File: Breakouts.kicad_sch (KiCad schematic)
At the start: 11 parts, among them J1 Conn_01x08, J2 Conn_01x08, J3 Conn_01x08, J4 Conn_01x08, J5 Conn_02x04_Odd_Even, J6 Conn_01x06, J7 Conn_01x06, K1 G5LE-1, U1 ESP-07, U2 AMS1117-3_3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

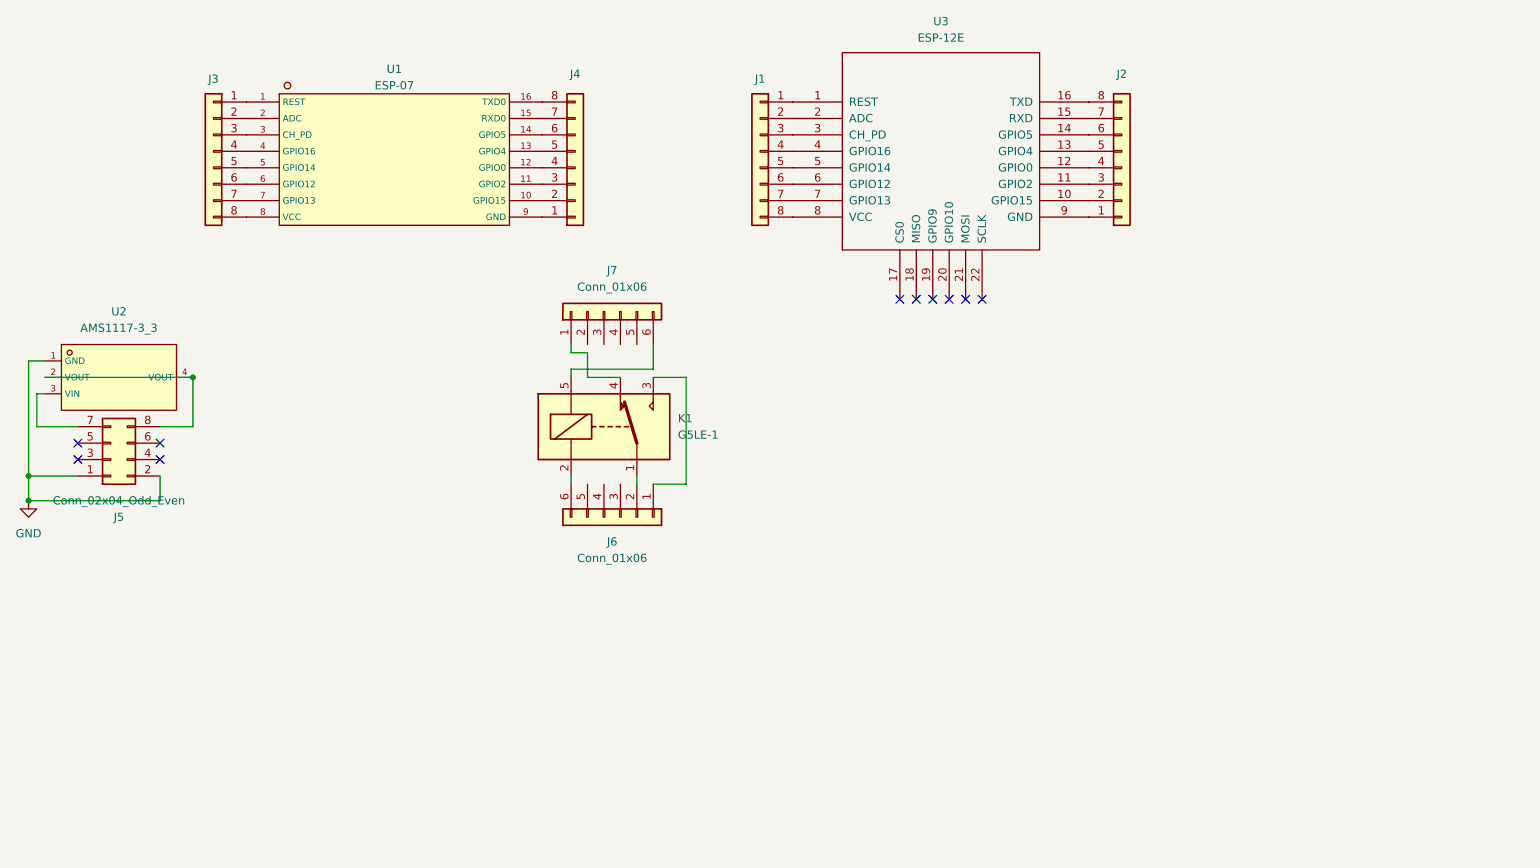
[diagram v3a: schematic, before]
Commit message: Add audio jack
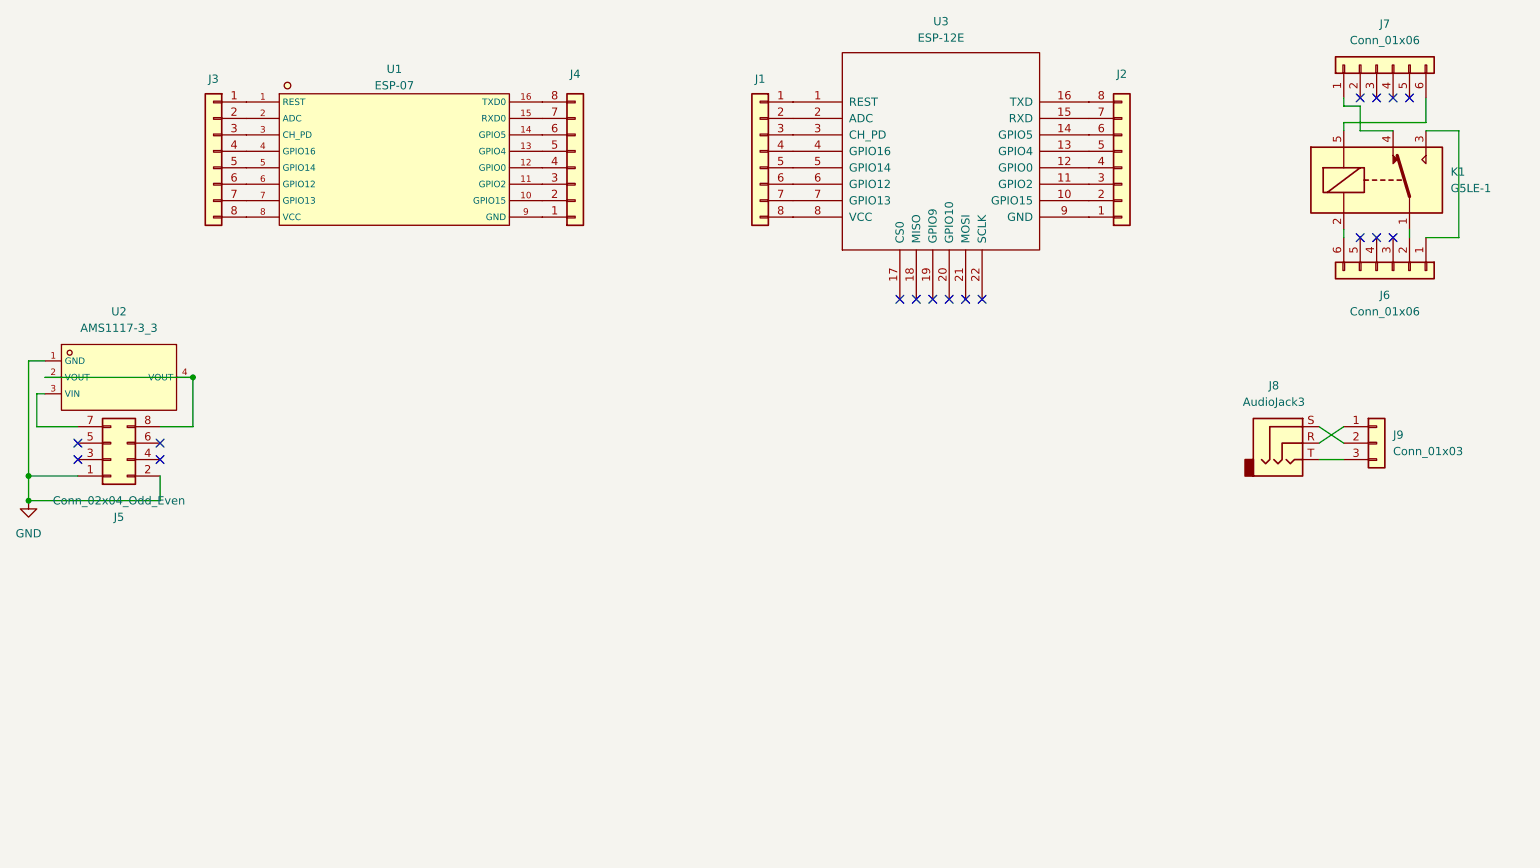
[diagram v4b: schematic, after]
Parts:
- added J8: AudioJack3, Connector_Audio:Jack_3.5mm_CUI_SJ-3523-SMT_Horizontal, symbol Connector_Audio:AudioJack3
- added J9: Conn_01x03, Connector_PinHeader_2.54mm:PinHeader_1x03_P2.54mm_Vertical, symbol Connector_Generic:Conn_01x03
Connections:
- new net: J8.R, J9.1 (Pin_1)
- new net: J8.S, J9.2 (Pin_2)
- new net: J8.T, J9.3 (Pin_3)
- no-connect marks 10 -> 17
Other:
- moved on the sheet: J6, J7, K1
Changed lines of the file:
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@@
   )
   (no_connect (at 193.04 59.055))
+  (no_connect (at 261.62 49.53))
+  (no_connect (at 261.62 27.94))
   (no_connect (at 63.5 83.82))
   (no_connect (at 76.2 81.28))
+  (no_connect (at 264.16 27.94))
   (no_connect (at 63.5 81.28))
   (no_connect (at 203.2 59.055))
+  (no_connect (at 269.24 27.94))
   (no_connect (at 76.2 83.82))
   (no_connect (at 190.5 59.055))
+  (no_connect (at 264.16 49.53))
   (no_connect (at 200.66 59.055))
   (no_connect (at 195.58 59.055))
+  (no_connect (at 266.7 49.53))
+  (no_connect (at 266.7 27.94))
   (no_connect (at 198.12 59.055))
-  (wire (pts (xy 139.7 67.31) (xy 139.7 66.04))
-    (stroke (width 0) (type default))
-  )
-  (wire (pts (xy 139.7 69.85) (xy 139.7 71.12))
-    (stroke (width 0) (type default))
-  )
-  (wire (pts (xy 142.24 67.31) (xy 139.7 67.31))
+  (wire (pts (xy 259.08 29.21) (xy 259.08 27.94))
+    (stroke (width 0) (type default))
+  )
+  (wire (pts (xy 259.08 31.75) (xy 259.08 33.02))
+    (stroke (width 0) (type default))
+  )
+  (wire (pts (xy 255.27 83.82) (xy 259.08 83.82))
+    (stroke (width 0) (type default))
+  )
+  (wire (pts (xy 261.62 29.21) (xy 259.08 29.21))
     (stroke (width 0) (type default))
   )
@@
     (stroke (width 0) (type default))
   )
-  (wire (pts (xy 152.4 69.85) (xy 139.7 69.85))
-    (stroke (width 0) (type default))
-  )
-  (wire (pts (xy 147.32 71.12) (xy 142.24 71.12))
+  (wire (pts (xy 271.78 31.75) (xy 259.08 31.75))
+    (stroke (width 0) (type default))
+  )
+  (wire (pts (xy 266.7 33.02) (xy 261.62 33.02))
     (stroke (width 0) (type default))
   )
@@
     (stroke (width 0) (type default))
   )
+  (wire (pts (xy 259.08 78.74) (xy 255.27 81.28))
+    (stroke (width 0) (type default))
+  )
   (wire (pts (xy 55.88 90.17) (xy 76.2 90.17))
     (stroke (width 0) (type default))
   )
-  (wire (pts (xy 142.24 71.12) (xy 142.24 67.31))
-    (stroke (width 0) (type default))
-  )
-  (wire (pts (xy 152.4 71.12) (xy 157.48 71.12))
+  (wire (pts (xy 261.62 33.02) (xy 261.62 29.21))
+    (stroke (width 0) (type default))
+  )
+  (wire (pts (xy 271.78 33.02) (xy 276.86 33.02))
     (stroke (width 0) (type default))
   )
@@
     (stroke (width 0) (type default))
   )
-  (wire (pts (xy 139.7 86.36) (xy 139.7 87.63))
+  (wire (pts (xy 259.08 48.26) (xy 259.08 49.53))
     (stroke (width 0) (type default))
   )
@@
     (stroke (width 0) (type default))
   )
-  (wire (pts (xy 157.48 71.12) (xy 157.48 87.63))
-    (stroke (width 0) (type default))
-  )
-  (wire (pts (xy 149.86 86.36) (xy 149.86 87.63))
-    (stroke (width 0) (type default))
-  )
-  (wire (pts (xy 152.4 66.04) (xy 152.4 69.85))
+  (wire (pts (xy 276.86 33.02) (xy 276.86 49.53))
+    (stroke (width 0) (type default))
+  )
+  (wire (pts (xy 269.24 48.26) (xy 269.24 49.53))
+    (stroke (width 0) (type default))
+  )
+  (wire (pts (xy 271.78 27.94) (xy 271.78 31.75))
     (stroke (width 0) (type default))
   )
@@
     (stroke (width 0) (type default))
   )
-  (wire (pts (xy 157.48 87.63) (xy 152.4 87.63))
+  (wire (pts (xy 276.86 49.53) (xy 271.78 49.53))
+    (stroke (width 0) (type default))
+  )
+  (wire (pts (xy 255.27 78.74) (xy 259.08 81.28))
     (stroke (width 0) (type default))
   )
@@
         (path "/7ebf650a-1c0b-4d71-8ef1-c883cde2ac89"
           (reference "U2") (unit 1)
+        )
+      )
+    )
+  )
+  (symbol (lib_id "Connector_Generic:Conn_01x03") (at 264.16 81.28 0) (unit 1)
+    (in_bom yes) (on_board yes) (dnp no) (fields_autoplaced)
+    (property "Reference" "J9" (at 266.7 80.01 0)
+      (effects (font (size 1.27 1.27)) (justify left))
+    )
+    (property "Value" "Conn_01x03" (at 266.7 82.55 0)
+      (effects (font (size 1.27 1.27)) (justify left))
+    )
+    (property "Footprint" "Connector_PinHeader_2.54mm:PinHeader_1x03_P2.54mm_Vertical" (at 264.16 81.28 0)
+      (effects (font (size 1.27 1.27)) hide)
+    )
+    (property "Datasheet" "~" (at 264.16 81.28 0)
+      (effects (font (size 1.27 1.27)) hide)
+    )
+    (pin "1")
+    (pin "3")
+    (pin "2")
+    (instances
+      (project "Breakouts"
+        (path "/7ebf650a-1c0b-4d71-8ef1-c883cde2ac89"
+          (reference "J9") (unit 1)
         )
       )
@@
     )
   )
-  (symbol (lib_id "Connector_Generic:Conn_01x06") (at 147.32 92.71 270) (unit 1)
-    (in_bom yes) (on_board yes) (dnp no) (fields_autoplaced)
-    (property "Reference" "J6" (at 146.05 96.52 90)
-      (effects (font (size 1.27 1.27)))
-    )
-    (property "Value" "Conn_01x06" (at 146.05 99.06 90)
-      (effects (font (size 1.27 1.27)))
-    )
-    (property "Footprint" "Connector_PinHeader_2.54mm:PinHeader_1x06_P2.54mm_Vertical" (at 147.32 92.71 0)
-      (effects (font (size 1.27 1.27)) hide)
-    )
-    (property "Datasheet" "~" (at 147.32 92.71 0)
+  (symbol (lib_id "Connector_Generic:Conn_01x06") (at 266.7 54.61 270) (unit 1)
+    (in_bom yes) (on_board yes) (dnp no) (fields_autoplaced)
+    (property "Reference" "J6" (at 265.43 58.42 90)
+      (effects (font (size 1.27 1.27)))
+    )
+    (property "Value" "Conn_01x06" (at 265.43 60.96 90)
+      (effects (font (size 1.27 1.27)))
+    )
+    (property "Footprint" "Connector_PinHeader_2.54mm:PinHeader_1x06_P2.54mm_Vertical" (at 266.7 54.61 0)
+      (effects (font (size 1.27 1.27)) hide)
+    )
+    (property "Datasheet" "~" (at 266.7 54.61 0)
       (effects (font (size 1.27 1.27)) hide)
     )
@@
     )
   )
-  (symbol (lib_id "Relay:G5LE-1") (at 144.78 78.74 0) (unit 1)
+  (symbol (lib_id "Relay:G5LE-1") (at 264.16 40.64 0) (unit 1)
     (in_bom no) (on_board yes) (dnp no) (fields_autoplaced)
-    (property "Reference" "K1" (at 156.21 77.47 0)
+    (property "Reference" "K1" (at 275.59 39.37 0)
       (effects (font (size 1.27 1.27)) (justify left))
     )
-    (property "Value" "G5LE-1" (at 156.21 80.01 0)
+    (property "Value" "G5LE-1" (at 275.59 41.91 0)
       (effects (font (size 1.27 1.27)) (justify left))
     )
-    (property "Footprint" "Relay_THT:Relay_SPDT_Omron-G5LE-1" (at 156.21 80.01 0)
+    (property "Footprint" "Relay_THT:Relay_SPDT_Omron-G5LE-1" (at 275.59 41.91 0)
       (effects (font (size 1.27 1.27)) (justify left) hide)
     )
-    (property "Datasheet" "http://www.omron.com/ecb/products/pdf/en-g5le.pdf" (at 144.78 78.74 0)
+    (property "Datasheet" "http://www.omron.com/ecb/products/pdf/en-g5le.pdf" (at 264.16 40.64 0)
       (effects (font (size 1.27 1.27)) hide)
     )
@@
     )
   )
-  (symbol (lib_id "Connector_Generic:Conn_01x06") (at 144.78 60.96 90) (unit 1)
-    (in_bom yes) (on_board yes) (dnp no) (fields_autoplaced)
-    (property "Reference" "J7" (at 146.05 54.61 90)
-      (effects (font (size 1.27 1.27)))
-    )
-    (property "Value" "Conn_01x06" (at 146.05 57.15 90)
-      (effects (font (size 1.27 1.27)))
-    )
-    (property "Footprint" "Connector_PinHeader_2.54mm:PinHeader_1x06_P2.54mm_Vertical" (at 144.78 60.96 0)
-      (effects (font (size 1.27 1.27)) hide)
-    )
-    (property "Datasheet" "~" (at 144.78 60.96 0)
+  (symbol (lib_id "Connector_Generic:Conn_01x06") (at 264.16 22.86 90) (unit 1)
+    (in_bom yes) (on_board yes) (dnp no) (fields_autoplaced)
+    (property "Reference" "J7" (at 265.43 16.51 90)
+      (effects (font (size 1.27 1.27)))
+    )
+    (property "Value" "Conn_01x06" (at 265.43 19.05 90)
+      (effects (font (size 1.27 1.27)))
+    )
+    (property "Footprint" "Connector_PinHeader_2.54mm:PinHeader_1x06_P2.54mm_Vertical" (at 264.16 22.86 0)
+      (effects (font (size 1.27 1.27)) hide)
+    )
+    (property "Datasheet" "~" (at 264.16 22.86 0)
       (effects (font (size 1.27 1.27)) hide)
     )
@@
         )
       )
+    )
+  )
+  (symbol (lib_id "Connector_Audio:AudioJack3") (at 250.19 81.28 0) (unit 1)
+    (in_bom yes) (on_board yes) (dnp no) (fields_autoplaced)
+    (property "Reference" "J8" (at 248.285 72.39 0)
+      (effects (font (size 1.27 1.27)))
+    )
+    (property "Value" "AudioJack3" (at 248.285 74.93 0)
+      (effects (font (size 1.27 1.27)))
+    )
+    (property "Footprint" "Connector_Audio:Jack_3.5mm_CUI_SJ-3523-SMT_Horizontal" (at 250.19 81.28 0)
+      (effects (font (size 1.27 1.27)) hide)
+    )
+    (property "Datasheet" "~" (at 250.19 81.28 0)
+      (effects (font (size 1.27 1.27)) hide)
+    )
+    (pin "T")
+    (pin "R")
+    (pin "S")
+    (instances
+      (project "Breakouts"
+        (path "/7ebf650a-1c0b-4d71-8ef1-c883cde2ac89"
+          (reference "J8") (unit 1)
+        )
+      )

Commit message: big audio jack
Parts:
- added J10: AudioJack3_Switch, Connector_Audio:Jack_6.35mm_Neutrik_NMJ6HFD2_Horizontal, symbol Connector_Audio:AudioJack3_Switch
- added J11, J12: Conn_01x03, Connector_PinHeader_2.54mm:PinHeader_1x03_P2.54mm_Vertical_SMD_Pin1Left, symbol Connector_Generic:Conn_01x03
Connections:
- new net: J10.S, J11.1 (Pin_1)
- new net: J10.R, J11.2 (Pin_2)
- new net: J10.T, J11.3 (Pin_3)
- new net: J10.TN, J12.1 (Pin_1)
- new net: J10.RN, J12.2 (Pin_2)
- new net: J10.SN, J12.3 (Pin_3)
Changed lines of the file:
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@@
+    (stroke (width 0) (type default))
+  )
+  (wire (pts (xy 214.63 102.87) (xy 217.17 102.87))
     (stroke (width 0) (type default))
   )
@@
     (stroke (width 0) (type default))
   )
+  (wire (pts (xy 218.44 97.79) (xy 218.44 105.41))
+    (stroke (width 0) (type default))
+  )
+  (wire (pts (xy 222.25 92.71) (xy 222.25 95.25))
+    (stroke (width 0) (type default))
+  )
   (wire (pts (xy 57.15 78.74) (xy 57.15 73.66))
     (stroke (width 0) (type default))
@@
     (stroke (width 0) (type default))
   )
+  (wire (pts (xy 218.44 105.41) (xy 224.79 105.41))
+    (stroke (width 0) (type default))
+  )
+  (wire (pts (xy 224.79 100.33) (xy 214.63 100.33))
+    (stroke (width 0) (type default))
+  )
+  (wire (pts (xy 222.25 95.25) (xy 214.63 95.25))
+    (stroke (width 0) (type default))
+  )
+  (wire (pts (xy 214.63 97.79) (xy 218.44 97.79))
+    (stroke (width 0) (type default))
+  )
+  (wire (pts (xy 217.17 107.95) (xy 224.79 107.95))
+    (stroke (width 0) (type default))
+  )
   (wire (pts (xy 58.42 68.58) (xy 55.88 68.58))
     (stroke (width 0) (type default))
   )
+  (wire (pts (xy 219.71 102.87) (xy 224.79 102.87))
+    (stroke (width 0) (type default))
+  )
   (wire (pts (xy 57.15 73.66) (xy 58.42 73.66))
     (stroke (width 0) (type default))
@@
     (stroke (width 0) (type default))
   )
+  (wire (pts (xy 224.79 92.71) (xy 222.25 92.71))
+    (stroke (width 0) (type default))
+  )
   (wire (pts (xy 81.28 78.74) (xy 76.2 78.74))
     (stroke (width 0) (type default))
   )
+  (wire (pts (xy 224.79 95.25) (xy 224.79 100.33))
+    (stroke (width 0) (type default))
+  )
   (wire (pts (xy 58.42 71.12) (xy 81.28 71.12))
     (stroke (width 0) (type default))
   )
+  (wire (pts (xy 224.79 90.17) (xy 214.63 90.17))
+    (stroke (width 0) (type default))
+  )
   (wire (pts (xy 276.86 33.02) (xy 276.86 49.53))
     (stroke (width 0) (type default))
@@
     (stroke (width 0) (type default))
   )
+  (wire (pts (xy 219.71 92.71) (xy 219.71 102.87))
+    (stroke (width 0) (type default))
+  )
   (wire (pts (xy 76.2 90.17) (xy 76.2 86.36))
+    (stroke (width 0) (type default))
+  )
+  (wire (pts (xy 217.17 102.87) (xy 217.17 107.95))
+    (stroke (width 0) (type default))
+  )
+  (wire (pts (xy 214.63 92.71) (xy 219.71 92.71))
     (stroke (width 0) (type default))
   )
@@
     )
   )
+  (symbol (lib_id "Connector_Generic:Conn_01x03") (at 229.87 92.71 0) (unit 1)
+    (in_bom yes) (on_board yes) (dnp no)
+    (property "Reference" "J11" (at 232.41 91.44 0)
+      (effects (font (size 1.27 1.27)) (justify left))
+    )
+    (property "Value" "Conn_01x03" (at 232.41 93.98 0)
+      (effects (font (size 1.27 1.27)) (justify left))
+    )
+    (property "Footprint" "Connector_PinHeader_2.54mm:PinHeader_1x03_P2.54mm_Vertical_SMD_Pin1Left" (at 229.87 92.71 0)
+      (effects (font (size 1.27 1.27)) hide)
+    )
+    (property "Datasheet" "~" (at 229.87 92.71 0)
+      (effects (font (size 1.27 1.27)) hide)
+    )
+    (pin "1")
+    (pin "2")
+    (pin "3")
+    (instances
+      (project "Breakouts"
+        (path "/7ebf650a-1c0b-4d71-8ef1-c883cde2ac89"
+          (reference "J11") (unit 1)
+        )
+      )
+    )
+  )
   (symbol (lib_id "jlc_symbols:ESP-07") (at 112.395 36.195 0) (unit 1)
     (in_bom yes) (on_board yes) (dnp no) (fields_autoplaced)
@@
     )
   )
+  (symbol (lib_id "Connector_Generic:Conn_01x03") (at 229.87 105.41 0) (mirror x) (unit 1)
+    (in_bom yes) (on_board yes) (dnp no)
+    (property "Reference" "J12" (at 232.41 106.68 0)
+      (effects (font (size 1.27 1.27)) (justify left))
+    )
+    (property "Value" "Conn_01x03" (at 232.41 104.14 0)
+      (effects (font (size 1.27 1.27)) (justify left))
+    )
+    (property "Footprint" "Connector_PinHeader_2.54mm:PinHeader_1x03_P2.54mm_Vertical_SMD_Pin1Left" (at 229.87 105.41 0)
+      (effects (font (size 1.27 1.27)) hide)
+    )
+    (property "Datasheet" "~" (at 229.87 105.41 0)
+      (effects (font (size 1.27 1.27)) hide)
+    )
+    (pin "1")
+    (pin "2")
+    (pin "3")
+    (instances
+      (project "Breakouts"
+        (path "/7ebf650a-1c0b-4d71-8ef1-c883cde2ac89"
+          (reference "J12") (unit 1)
+        )
+      )
+    )
+  )
   (symbol (lib_id "Connector_Generic:Conn_01x08") (at 140.335 38.735 0) (mirror x) (unit 1)
     (in_bom yes) (on_board yes) (dnp no) (fields_autoplaced)
@@
         )
       )
+    )
+  )
+  (symbol (lib_id "Connector_Audio:AudioJack3_Switch") (at 209.55 95.25 0) (unit 1)
+    (in_bom yes) (on_board yes) (dnp no) (fields_autoplaced)
+    (property "Reference" "J10" (at 207.645 83.82 0)
+      (effects (font (size 1.27 1.27)))
+    )
+    (property "Value" "AudioJack3_Switch" (at 207.645 86.36 0)
+      (effects (font (size 1.27 1.27)))
+    )
+    (property "Footprint" "Connector_Audio:Jack_6.35mm_Neutrik_NMJ6HFD2_Horizontal" (at 209.55 95.25 0)
+      (effects (font (size 1.27 1.27)) hide)
+    )
+    (property "Datasheet" "~" (at 209.55 95.25 0)
+      (effects (font (size 1.27 1.27)) hide)
+    )
+    (pin "RN")
+    (pin "TN")
+    (pin "SN")
+    (pin "T")
+    (pin "R")
+    (pin "S")
+    (instances
+      (project "Breakouts"
+        (path "/7ebf650a-1c0b-4d71-8ef1-c883cde2ac89"
+          (reference "J10") (unit 1)
+        )
+      )
